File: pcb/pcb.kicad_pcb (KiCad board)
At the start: 2 copper layers, 53 x 73 mm, 129 parts, among them J1 I2C_Data, J2 SPI_Flash, SW1 Select, SW2 Done, U1 ATmega328P-AU, U2 HotelPasteur-V4.0, Y1 16Mhz

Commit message: Fix LED naming and parsing script for SMD components
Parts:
- renumbered D110 to D91

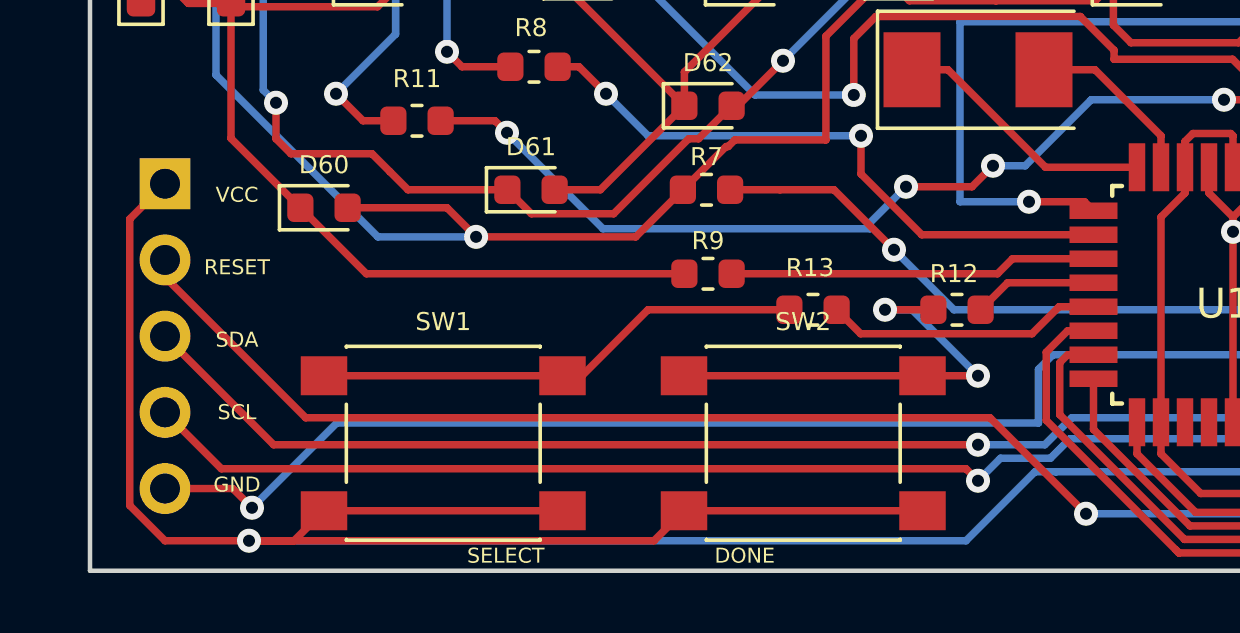
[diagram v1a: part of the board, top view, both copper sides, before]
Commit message: fix buttons gnd
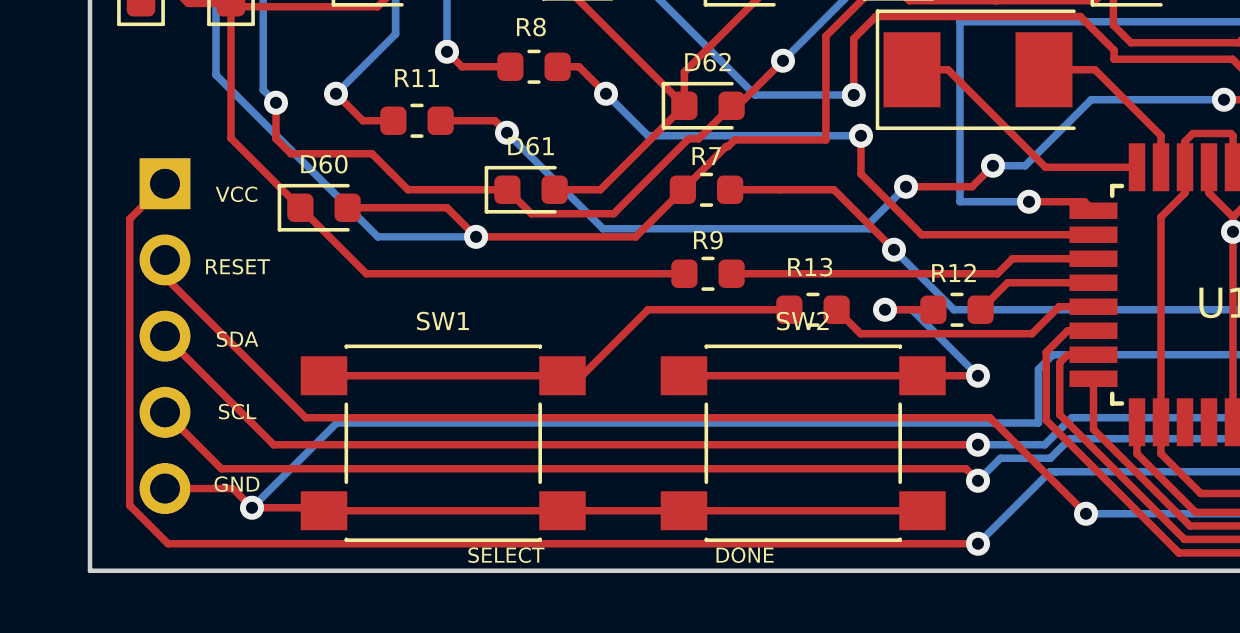
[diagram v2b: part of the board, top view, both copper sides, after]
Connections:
- SW1 pad 2: Net-(J1-Pad1) -> GND
- SW2 pad 2: Net-(J1-Pad1) -> GND
- U1 pad 19: (no net) -> Net-(U1-Pad19)
- U1 pad 20: (no net) -> Net-(U1-Pad20)
- U1 pad 22: (no net) -> Net-(U1-Pad22)
- U1 pad 26: (no net) -> Net-(U1-Pad26)
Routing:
- net Net-(J1-Pad1): track 117.6 -> 83.5 mm
- net GND: track 71.5 -> 94.4 mm
